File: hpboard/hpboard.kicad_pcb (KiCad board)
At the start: 2 copper layers, 60 x 100 mm, 28 parts, among them Q1 T2N7002AK, Q2 T2N7002AK, Q3 Si4435FDY, Q4 Si4435FDY, SW1 FSM2JAH, U1 TMCS1108A4B, U2 ATtiny1604-SS, U3 TLV1117-50

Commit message: Design heating plate
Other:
- board text added: "12V/5Amp"
- board text added: "GND"
- board text added: "Hotplate controller Rev. 1 github.com/c0pperdragon/HotPlate"
- board text added: "UDPI"

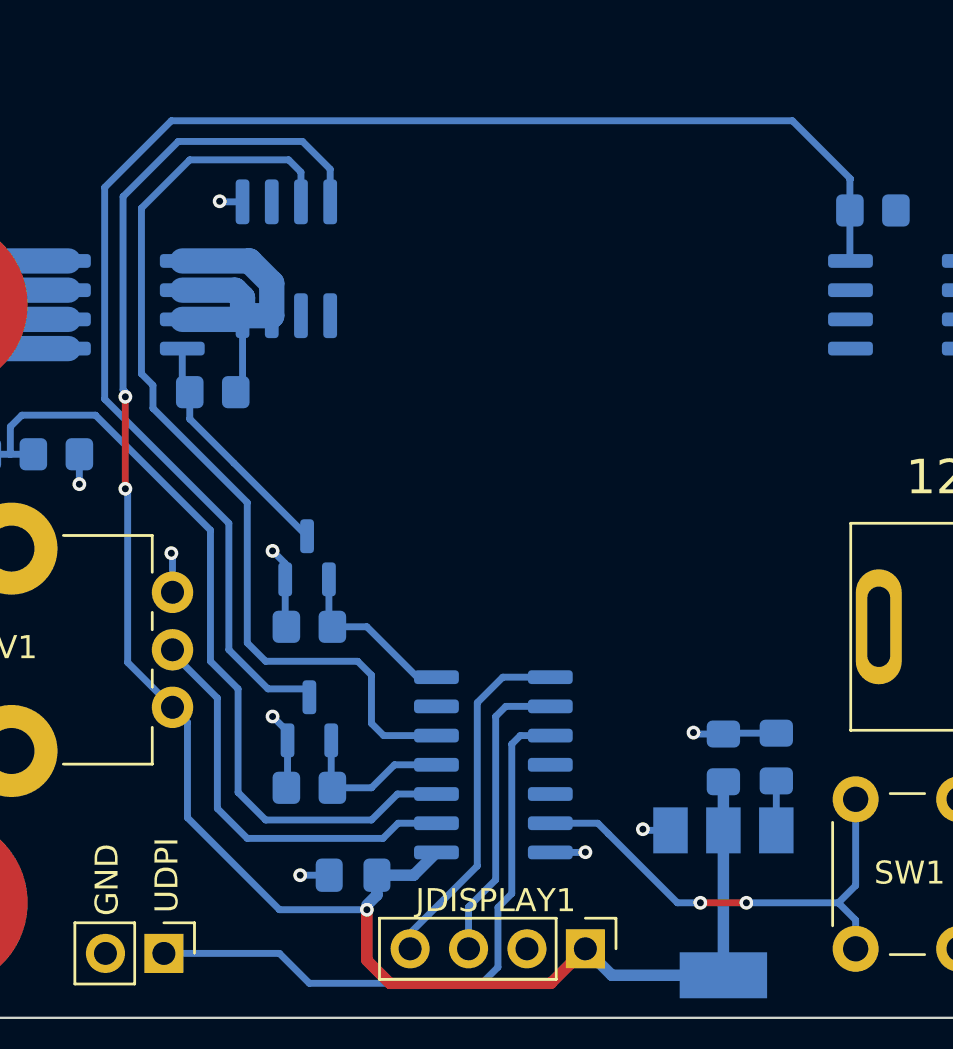
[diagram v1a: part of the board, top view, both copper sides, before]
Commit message: Add some space between ICs
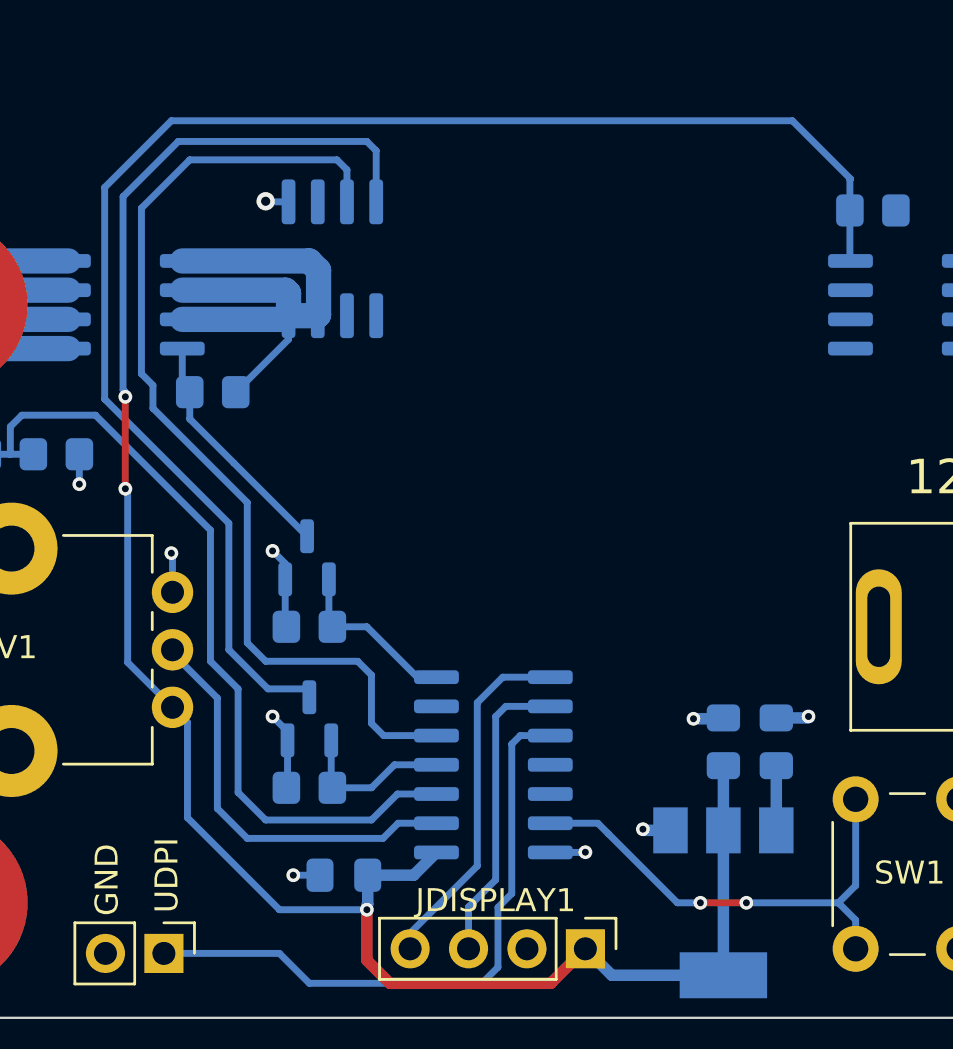
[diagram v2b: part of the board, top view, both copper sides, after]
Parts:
- moved U1 2.00 mm to (122.0, 115.0)
- moved C2 0.70 mm to (139.0, 136.0)
- moved C1 0.66 mm to (141.3, 136.0)
- moved C3 0.40 mm to (122.5, 141.8)
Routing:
- net Net-(U1-Pad3): track 16.6 -> 24.0 mm
- net +5V: track 81.8 -> 85.2 mm
- net /SENSE_CURRENT: track 41.2 -> 43.3 mm
- net GND: track 18.6 -> 17.6 mm, vias 9 -> 10
- net /12V: track 2.15 -> 2.81 mm

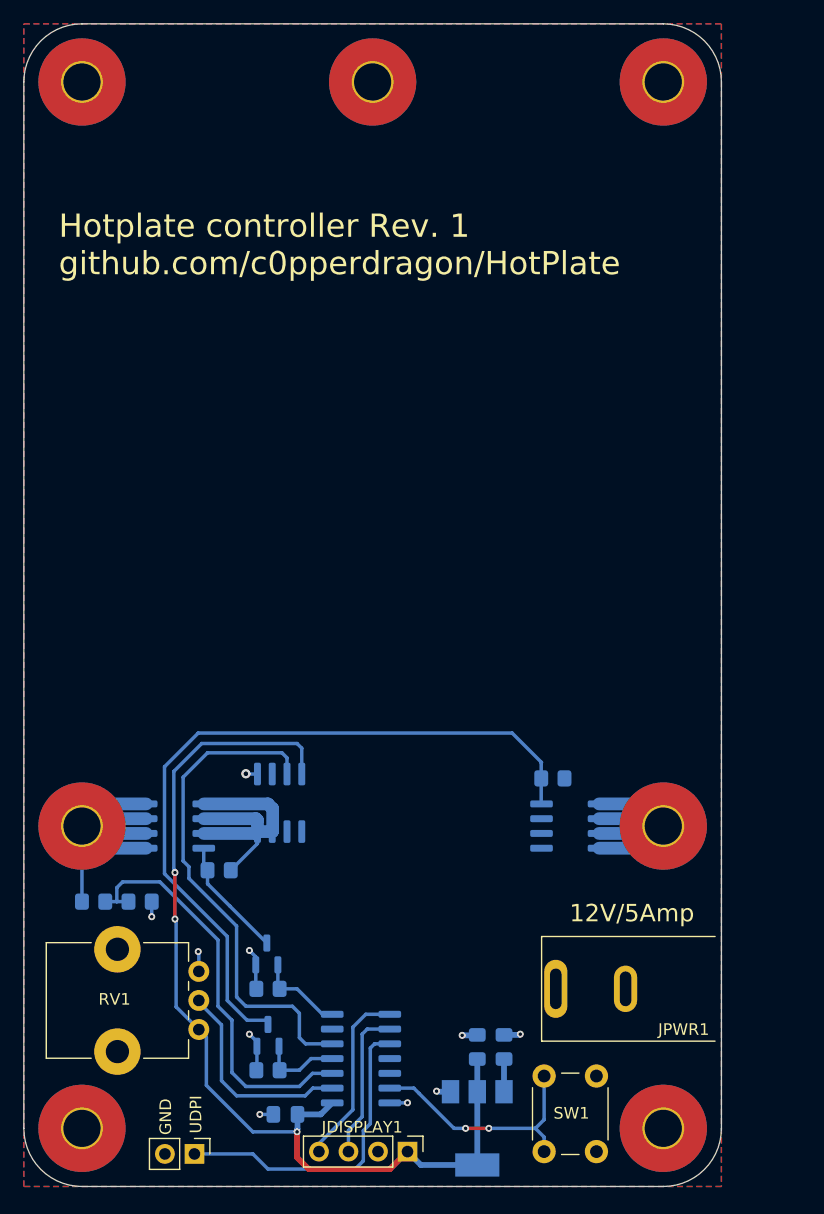
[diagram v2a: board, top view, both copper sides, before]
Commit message: Less noise in current sensing. Faster regulation.
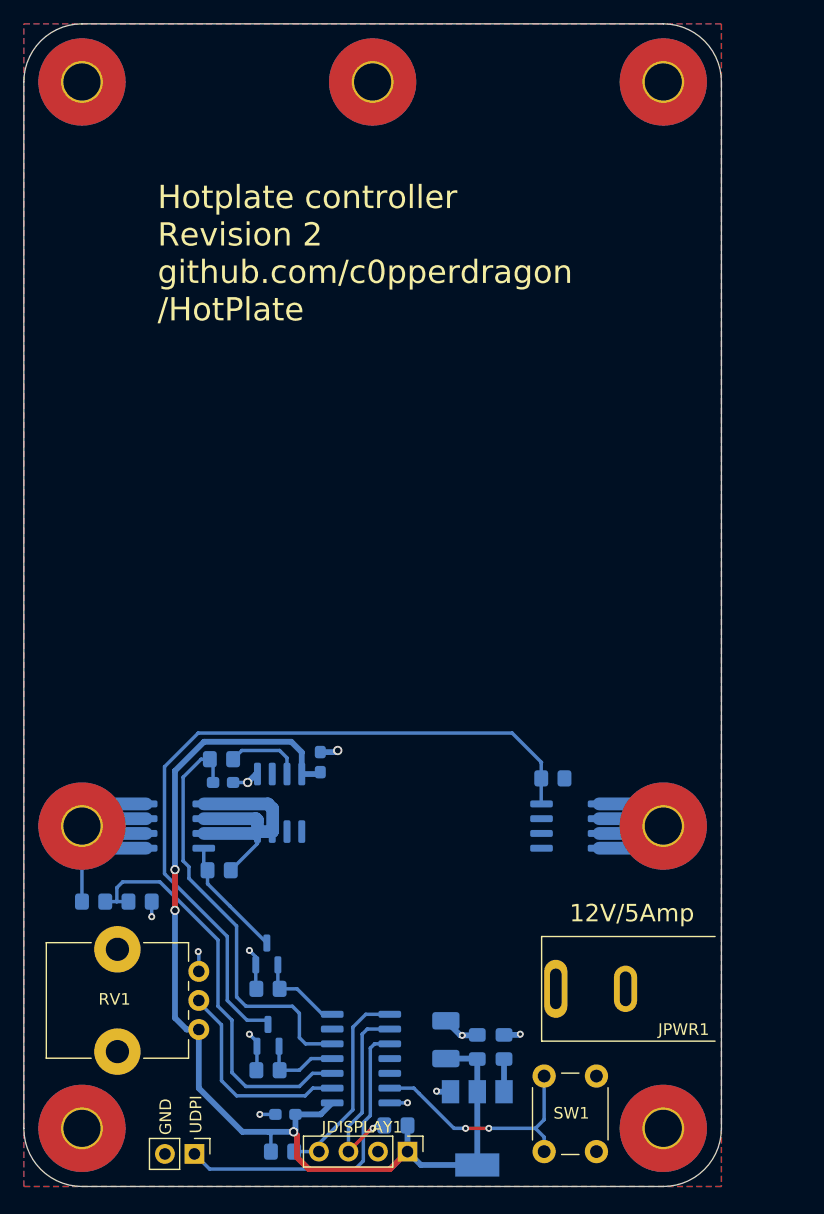
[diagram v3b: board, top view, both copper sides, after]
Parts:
- added C4: 100uF, Capacitor_Tantalum_SMD:CP_EIA-3528-21_Kemet-B_Pad1.50x2.35mm_HandSolder, B.Cu at (136.3, 135.4)
- added C5: 100nF, Capacitor_SMD:C_0603_1608Metric_Pad1.08x0.95mm_HandSolder, B.Cu at (125.5, 111.5)
- added C6: 100nF, Capacitor_SMD:C_0603_1608Metric_Pad1.08x0.95mm_HandSolder, B.Cu at (117.1, 113.2)
- added R7: 10k, Resistor_SMD:R_0805_2012Metric_Pad1.20x1.40mm_HandSolder, B.Cu at (132.0, 142.8)
- added R8: 10k, Resistor_SMD:R_0805_2012Metric_Pad1.20x1.40mm_HandSolder, B.Cu at (122.2, 145.0)
- added R9: 1k, Resistor_SMD:R_0805_2012Metric_Pad1.20x1.40mm_HandSolder, B.Cu at (117.0, 111.2)
- C1: value 1uF -> 10uF
- C3: footprint Capacitor_SMD:C_0805_2012Metric_Pad1.18x1.45mm_HandSolder -> Capacitor_SMD:C_0603_1608Metric_Pad1.08x0.95mm_HandSolder
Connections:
- U1 pad 7: /SENSE_CURRENT -> Net-(U1-Pad7)
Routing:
- net +5V: track 85.2 -> 94.5 mm
- net Net-(U1-Pad7): track 0.00 -> 6.60 mm
- net /SENSE_CURRENT: track 43.3 -> 37.0 mm
- net GND: track 17.6 -> 22.5 mm, vias 10 -> 11
- net /SCL: track 13.1 -> 17.2 mm, vias 0 -> 1
- net /SDA: track 15.5 -> 17.7 mm
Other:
- board text added: "Hotplate controller Revision 2 github.com/c0pperdragon /HotPlate"
- board text removed: "Hotplate controller Rev. 1 github.com/c0pperdragon/HotPlate"

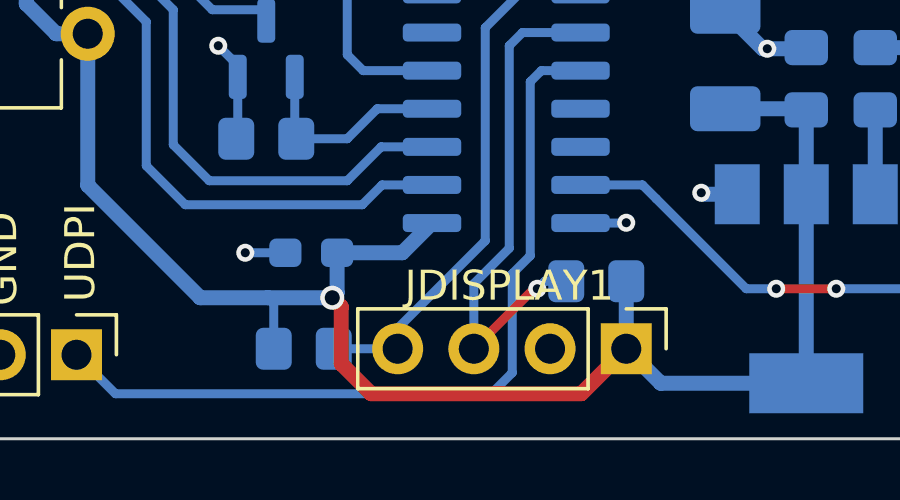
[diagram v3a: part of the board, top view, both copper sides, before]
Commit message: Remove unnecessary pull-ups
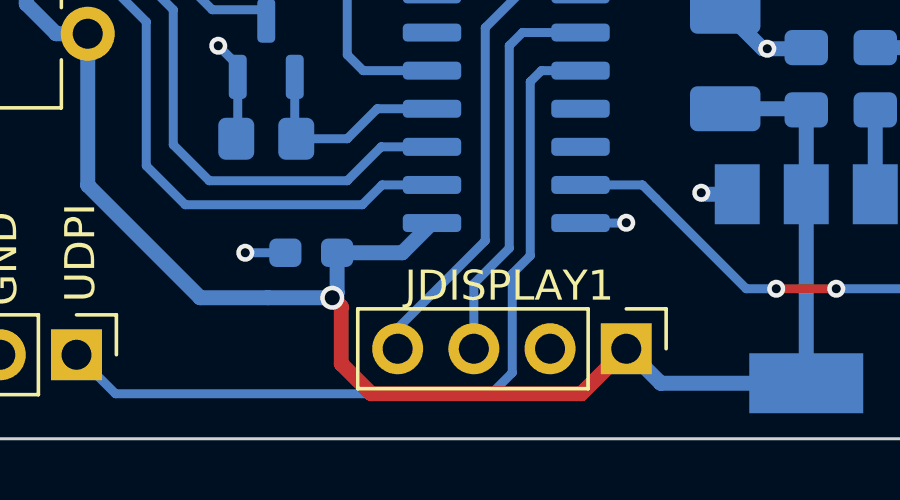
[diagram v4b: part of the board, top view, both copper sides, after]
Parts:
- removed R7, R8: 10k, Resistor_SMD:R_0805_2012Metric_Pad1.20x1.40mm_HandSolder
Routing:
- net +5V: track 94.5 -> 90.4 mm
- net /SCL: track 17.2 -> 13.1 mm, vias 1 -> 0
- net /SDA: track 17.7 -> 15.5 mm
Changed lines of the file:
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@@
   (net 24 "unconnected-(U2-Pad11)")
   (net 25 "unconnected-(U2-Pad6)")
-  (net 26 "Net-(U1-Pad7)")
+  (net 26 "Net-(R9-Pad1)")
   (footprint "Library:MountingHole_3.2mm_Large" (layer "F.Cu")
     (at 155 117)
@@
       (net 13 "unconnected-(U1-Pad6)") (pinfunction "N.C.") (pintype "passive+no_connect"))
     (pad "7" smd roundrect (at 2.475 0.635 90) (size 1.95 0.6) (layers "B.Cu" "B.Paste" "B.Mask") (roundrect_rratio 0.25)
-      (net 26 "Net-(U1-Pad7)") (pinfunction "VIOUT") (pintype "output"))
+      (net 26 "Net-(R9-Pad1)") (pinfunction "VIOUT") (pintype "output"))
     (pad "8" smd roundrect (at 2.475 1.905 90) (size 1.95 0.6) (layers "B.Cu" "B.Paste" "B.Mask") (roundrect_rratio 0.25)
       (net 1 "+5V") (pinfunction "VCC") (pintype "power_in"))
@@
     (fp_line (start 1 0.625) (end 1 -0.625) (layer "B.Fab") (width 0.1))
     (pad "1" smd roundrect (at -1 0 180) (size 1.2 1.4) (layers "B.Cu" "B.Paste" "B.Mask") (roundrect_rratio 0.208333)
-      (net 26 "Net-(U1-Pad7)") (pintype "passive"))
+      (net 26 "Net-(R9-Pad1)") (pintype "passive"))
     (pad "2" smd roundrect (at 1 0 180) (size 1.2 1.4) (layers "B.Cu" "B.Paste" "B.Mask") (roundrect_rratio 0.208333)
       (net 14 "/SENSE_CURRENT") (pintype "passive"))
@@
     )
   )
-  (footprint "Resistor_SMD:R_0805_2012Metric_Pad1.20x1.40mm_HandSolder" (layer "B.Cu")
-    (at 122.25 145 180)
-    (descr "Resistor SMD 0805 (2012 Metric), square (rectangular) end terminal, IPC_7351 nominal with elongated pad for handsoldering. (Body size source: IPC-SM-782 page 72, https://www.pcb-3d.com/wordpress/wp-content/uploads/ipc-sm-782a_amendment_1_and_2.pdf), generated with kicad-footprint-generator")
-    (tags "resistor handsolder")
-    (property "Sheetfile" "hpboard.kicad_sch")
-    (property "Sheetname" "")
-    (attr smd)
-    (fp_text reference "R8" (at 0 1.5) (layer "B.SilkS")
-      (effects (font (size 1 1) (thickness 0.15)) (justify mirror))
-    )
-    (fp_text value "10k" (at 0 -1.65) (layer "B.Fab")
-      (effects (font (size 1 1) (thickness 0.15)) (justify mirror))
-    )
-    (fp_text user "${REFERENCE}" (at 0 0) (layer "B.Fab")
-      (effects (font (size 0.5 0.5) (thickness 0.08)) (justify mirror))
-    )
-    (fp_line (start -0.227064 0.735) (end 0.227064 0.735) (layer "B.SilkS") (width 0.12))
-    (fp_line (start -0.227064 -0.735) (end 0.227064 -0.735) (layer "B.SilkS") (width 0.12))
-    (fp_line (start -1.85 0.95) (end 1.85 0.95) (layer "B.CrtYd") (width 0.05))
-    (fp_line (start 1.85 -0.95) (end -1.85 -0.95) (layer "B.CrtYd") (width 0.05))
-    (fp_line (start 1.85 0.95) (end 1.85 -0.95) (layer "B.CrtYd") (width 0.05))
-    (fp_line (start -1.85 -0.95) (end -1.85 0.95) (layer "B.CrtYd") (width 0.05))
-    (fp_line (start 1 -0.625) (end -1 -0.625) (layer "B.Fab") (width 0.1))
-    (fp_line (start 1 0.625) (end 1 -0.625) (layer "B.Fab") (width 0.1))
-    (fp_line (start -1 -0.625) (end -1 0.625) (layer "B.Fab") (width 0.1))
-    (fp_line (start -1 0.625) (end 1 0.625) (layer "B.Fab") (width 0.1))
-    (pad "1" smd roundrect (at -1 0 180) (size 1.2 1.4) (layers "B.Cu" "B.Paste" "B.Mask") (roundrect_rratio 0.208333)
-      (net 6 "/SDA") (pintype "passive"))
-    (pad "2" smd roundrect (at 1 0 180) (size 1.2 1.4) (layers "B.Cu" "B.Paste" "B.Mask") (roundrect_rratio 0.208333)
-      (net 1 "+5V") (pintype "passive"))
-    (model "${KICAD6_3DMODEL_DIR}/Resistor_SMD.3dshapes/R_0805_2012Metric.wrl"
-      (offset (xyz 0 0 0))
-      (scale (xyz 1 1 1))
-      (rotate (xyz 0 0 0))
-    )
-  )
   (footprint "Capacitor_SMD:C_0805_2012Metric_Pad1.18x1.45mm_HandSolder" (layer "B.Cu")
     (at 139 136 90)
@@
     )
   )
-  (footprint "Resistor_SMD:R_0805_2012Metric_Pad1.20x1.40mm_HandSolder" (layer "B.Cu")
-    (at 132 142.75)
-    (descr "Resistor SMD 0805 (2012 Metric), square (rectangular) end terminal, IPC_7351 nominal with elongated pad for handsoldering. (Body size source: IPC-SM-782 page 72, https://www.pcb-3d.com/wordpress/wp-content/uploads/ipc-sm-782a_amendment_1_and_2.pdf), generated with kicad-footprint-generator")
-    (tags "resistor handsolder")
-    (property "Sheetfile" "hpboard.kicad_sch")
-    (property "Sheetname" "")
-    (attr smd)
-    (fp_text reference "R7" (at -3.25 0.25) (layer "B.SilkS")
-      (effects (font (size 1 1) (thickness 0.15)) (justify mirror))
-    )
-    (fp_text value "10k" (at 0 -1.65) (layer "B.Fab")
-      (effects (font (size 1 1) (thickness 0.15)) (justify mirror))
-    )
-    (fp_text user "${REFERENCE}" (at 0 0) (layer "B.Fab")
-      (effects (font (size 0.5 0.5) (thickness 0.08)) (justify mirror))
-    )
-    (fp_line (start -0.227064 0.735) (end 0.227064 0.735) (layer "B.SilkS") (width 0.12))
-    (fp_line (start -0.227064 -0.735) (end 0.227064 -0.735) (layer "B.SilkS") (width 0.12))
-    (fp_line (start -1.85 -0.95) (end -1.85 0.95) (layer "B.CrtYd") (width 0.05))
-    (fp_line (start 1.85 -0.95) (end -1.85 -0.95) (layer "B.CrtYd") (width 0.05))
-    (fp_line (start -1.85 0.95) (end 1.85 0.95) (layer "B.CrtYd") (width 0.05))
-    (fp_line (start 1.85 0.95) (end 1.85 -0.95) (layer "B.CrtYd") (width 0.05))
-    (fp_line (start 1 0.625) (end 1 -0.625) (layer "B.Fab") (width 0.1))
-    (fp_line (start 1 -0.625) (end -1 -0.625) (layer "B.Fab") (width 0.1))
-    (fp_line (start -1 -0.625) (end -1 0.625) (layer "B.Fab") (width 0.1))
-    (fp_line (start -1 0.625) (end 1 0.625) (layer "B.Fab") (width 0.1))
-    (pad "1" smd roundrect (at -1 0) (size 1.2 1.4) (layers "B.Cu" "B.Paste" "B.Mask") (roundrect_rratio 0.208333)
-      (net 5 "/SCL") (pintype "passive"))
-    (pad "2" smd roundrect (at 1 0) (size 1.2 1.4) (layers "B.Cu" "B.Paste" "B.Mask") (roundrect_rratio 0.208333)
-      (net 1 "+5V") (pintype "passive"))
-    (model "${KICAD6_3DMODEL_DIR}/Resistor_SMD.3dshapes/R_0805_2012Metric.wrl"
-      (offset (xyz 0 0 0))
-      (scale (xyz 1 1 1))
-      (rotate (xyz 0 0 0))
-    )
-  )
   (footprint "Capacitor_SMD:C_0603_1608Metric_Pad1.08x0.95mm_HandSolder" (layer "B.Cu")
     (at 117.1375 113.25)
@@
   (segment (start 139 146.15) (end 134.15 146.15) (width 0.5) (layer "B.Cu") (net 1))
   (segment (start 139 139.85) (end 139 146.15) (width 0.5) (layer "B.Cu") (net 1))
-  (segment (start 121.25 145) (end 121.25 143.5) (width 0.3) (layer "B.Cu") (net 1))
   (segment (start 138.9625 137) (end 139 137.0375) (width 0.5) (layer "B.Cu") (net 1))
   (segment (start 123.905 112.525) (end 125.3375 112.525) (width 0.5) (layer "B.Cu") (net 1))
@@
   (segment (start 113 133.5) (end 114 134.5) (width 0.5) (layer "B.Cu") (net 1))
   (segment (start 115.5 109.75) (end 113 112.25) (width 0.5) (layer "B.Cu") (net 1))
-  (segment (start 133 145) (end 133 142.75) (width 0.5) (layer "B.Cu") (net 1))
-  (segment (start 121.25 143.5) (end 121.05 143.3) (width 0.3) (layer "B.Cu") (net 1))
   (via (at 142.7 134.9) (size 0.6) (drill 0.3) (layers "F.Cu" "B.Cu") (net 2))
   (via (at 111 124.8) (size 0.6) (drill 0.3) (layers "F.Cu" "B.Cu") (net 2))
@@
   (segment (start 149.475 115.095) (end 153.095 115.095) (width 1.1) (layer "B.Cu") (net 4))
   (segment (start 153.095 115.095) (end 155 117) (width 1.1) (layer "B.Cu") (net 4))
-  (segment (start 130.034266 143) (end 129.92 143) (width 0.3) (layer "F.Cu") (net 5))
-  (segment (start 129.92 143) (end 127.92 145) (width 0.3) (layer "F.Cu") (net 5))
-  (via (at 130.034266 143) (size 0.6) (drill 0.3) (layers "F.Cu" "B.Cu") (net 5))
   (segment (start 129.1 134.9) (end 129.1 141.65) (width 0.3) (layer "B.Cu") (net 5))
-  (segment (start 130.034266 143) (end 130.284266 142.75) (width 0.3) (layer "B.Cu") (net 5))
   (segment (start 127.92 142.83) (end 127.92 145) (width 0.3) (layer "B.Cu") (net 5))
   (segment (start 129.54 134.46) (end 129.1 134.9) (width 0.3) (layer "B.Cu") (net 5))
   (segment (start 131.475 134.46) (end 129.54 134.46) (width 0.3) (layer "B.Cu") (net 5))
-  (segment (start 130.284266 142.75) (end 131 142.75) (width 0.3) (layer "B.Cu") (net 5))
   (segment (start 129.1 141.65) (end 127.92 142.83) (width 0.3) (layer "B.Cu") (net 5))
   (segment (start 129.41 133.19) (end 128.3 134.3) (width 0.3) (layer "B.Cu") (net 6))
   (segment (start 128.3 141.4) (end 125.38 144.32) (width 0.3) (layer "B.Cu") (net 6))
   (segment (start 125.38 144.32) (end 125.38 145) (width 0.3) (layer "B.Cu") (net 6))
-  (segment (start 123.25 145) (end 125.38 145) (width 0.3) (layer "B.Cu") (net 6))
   (segment (start 131.475 133.19) (end 129.41 133.19) (width 0.3) (layer "B.Cu") (net 6))
   (segment (start 128.3 134.3) (end 128.3 141.4) (width 0.3) (layer "B.Cu") (net 6))
